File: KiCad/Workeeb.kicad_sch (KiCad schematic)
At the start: 224 parts, among them J1 USB_C_Receptacle_USB2.0, U1 EFM32HG322F64G-C-QFP48

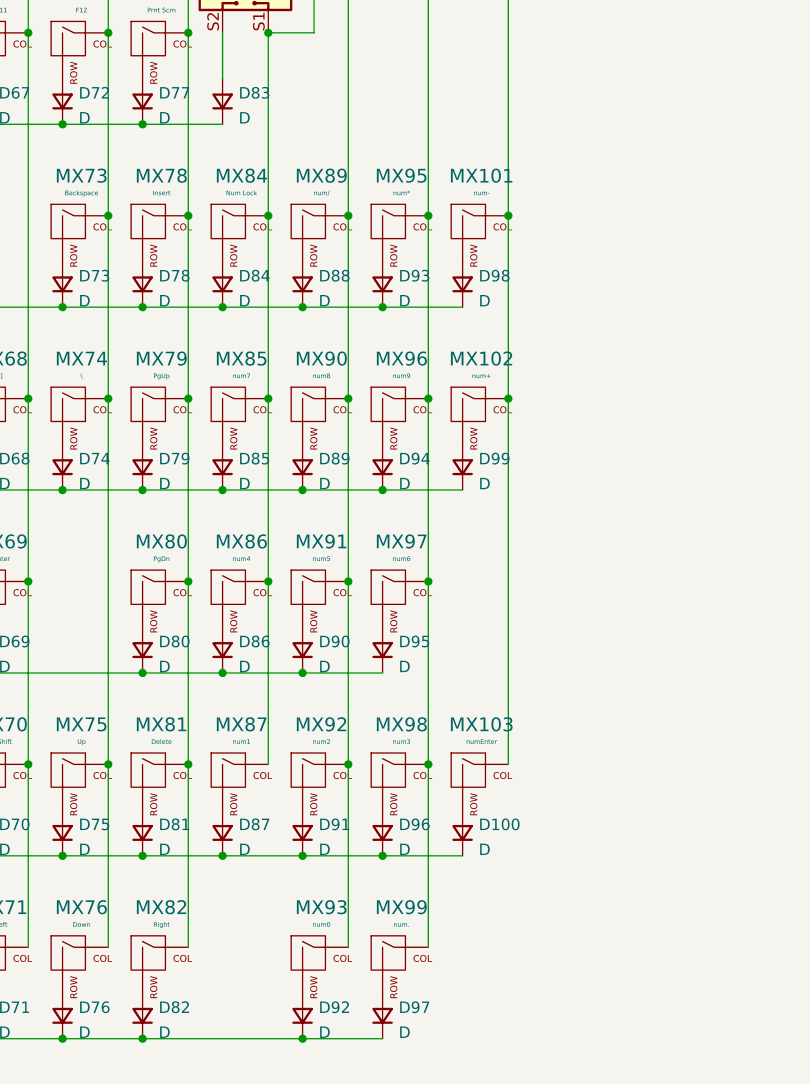
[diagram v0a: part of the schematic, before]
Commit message: Place all diodes and fix switch annotations
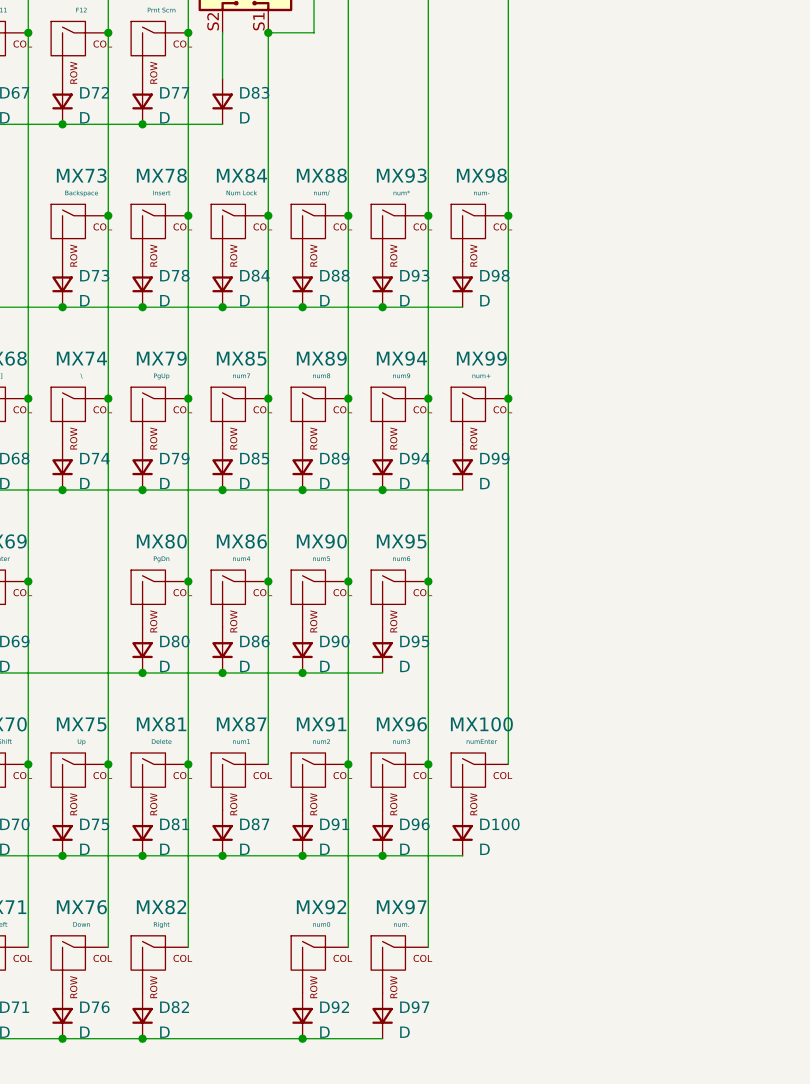
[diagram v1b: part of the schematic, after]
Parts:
- renumbered MX103 to MX100, MX89 to MX88, MX90 to MX89, MX91 to MX90, MX92 to MX91, MX93 to MX92, MX95 to MX93, MX96 to MX94, MX97 to MX95, MX98 to MX96, MX99 to MX97, MX101 to MX98, MX102 to MX99
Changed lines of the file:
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@@
   (symbol (lib_id "Workeeb-rescue:MX-NoLED-MX_Alps_Hybrid") (at 184.15 59.69 0) (unit 1)
     (in_bom yes) (on_board yes)
-    (property "Reference" "MX89" (id 0) (at 184.9882 54.0258 0)
+    (property "Reference" "MX88" (id 0) (at 184.9882 54.0258 0)
       (effects (font (size 1.524 1.524)))
     )
@@
   (symbol (lib_id "Workeeb-rescue:MX-NoLED-MX_Alps_Hybrid") (at 184.15 80.01 0) (unit 1)
     (in_bom yes) (on_board yes)
-    (property "Reference" "MX90" (id 0) (at 184.9882 74.3458 0)
+    (property "Reference" "MX89" (id 0) (at 184.9882 74.3458 0)
       (effects (font (size 1.524 1.524)))
     )
@@
   (symbol (lib_id "Workeeb-rescue:MX-NoLED-MX_Alps_Hybrid") (at 184.15 100.33 0) (unit 1)
     (in_bom yes) (on_board yes)
-    (property "Reference" "MX91" (id 0) (at 184.9882 94.6658 0)
+    (property "Reference" "MX90" (id 0) (at 184.9882 94.6658 0)
       (effects (font (size 1.524 1.524)))
     )
@@
   (symbol (lib_id "Workeeb-rescue:MX-NoLED-MX_Alps_Hybrid") (at 184.15 120.65 0) (unit 1)
     (in_bom yes) (on_board yes)
-    (property "Reference" "MX92" (id 0) (at 184.9882 114.9858 0)
+    (property "Reference" "MX91" (id 0) (at 184.9882 114.9858 0)
       (effects (font (size 1.524 1.524)))
     )
@@
   (symbol (lib_id "Workeeb-rescue:MX-NoLED-MX_Alps_Hybrid") (at 184.15 140.97 0) (unit 1)
     (in_bom yes) (on_board yes)
-    (property "Reference" "MX93" (id 0) (at 184.9882 135.3058 0)
+    (property "Reference" "MX92" (id 0) (at 184.9882 135.3058 0)
       (effects (font (size 1.524 1.524)))
     )
@@
   (symbol (lib_id "Workeeb-rescue:MX-NoLED-MX_Alps_Hybrid") (at 193.04 59.69 0) (unit 1)
     (in_bom yes) (on_board yes)
-    (property "Reference" "MX95" (id 0) (at 193.8782 54.0258 0)
+    (property "Reference" "MX93" (id 0) (at 193.8782 54.0258 0)
       (effects (font (size 1.524 1.524)))
     )
@@
   (symbol (lib_id "Workeeb-rescue:MX-NoLED-MX_Alps_Hybrid") (at 193.04 80.01 0) (unit 1)
     (in_bom yes) (on_board yes)
-    (property "Reference" "MX96" (id 0) (at 193.8782 74.3458 0)
+    (property "Reference" "MX94" (id 0) (at 193.8782 74.3458 0)
       (effects (font (size 1.524 1.524)))
     )
@@
   (symbol (lib_id "Workeeb-rescue:MX-NoLED-MX_Alps_Hybrid") (at 193.04 100.33 0) (unit 1)
     (in_bom yes) (on_board yes)
-    (property "Reference" "MX97" (id 0) (at 193.8782 94.6658 0)
+    (property "Reference" "MX95" (id 0) (at 193.8782 94.6658 0)
       (effects (font (size 1.524 1.524)))
     )
@@
   (symbol (lib_id "Workeeb-rescue:MX-NoLED-MX_Alps_Hybrid") (at 193.04 120.65 0) (unit 1)
     (in_bom yes) (on_board yes)
-    (property "Reference" "MX98" (id 0) (at 193.8782 114.9858 0)
+    (property "Reference" "MX96" (id 0) (at 193.8782 114.9858 0)
       (effects (font (size 1.524 1.524)))
     )
@@
   (symbol (lib_id "Workeeb-rescue:MX-NoLED-MX_Alps_Hybrid") (at 193.04 140.97 0) (unit 1)
     (in_bom yes) (on_board yes)
-    (property "Reference" "MX99" (id 0) (at 193.8782 135.3058 0)
+    (property "Reference" "MX97" (id 0) (at 193.8782 135.3058 0)
       (effects (font (size 1.524 1.524)))
     )
@@
   (symbol (lib_id "Workeeb-rescue:MX-NoLED-MX_Alps_Hybrid") (at 201.93 59.69 0) (unit 1)
     (in_bom yes) (on_board yes)
-    (property "Reference" "MX101" (id 0) (at 202.7682 54.0258 0)
+    (property "Reference" "MX98" (id 0) (at 202.7682 54.0258 0)
       (effects (font (size 1.524 1.524)))
     )
@@
   (symbol (lib_id "Workeeb-rescue:MX-NoLED-MX_Alps_Hybrid") (at 201.93 80.01 0) (unit 1)
     (in_bom yes) (on_board yes)
-    (property "Reference" "MX102" (id 0) (at 202.7682 74.3458 0)
+    (property "Reference" "MX99" (id 0) (at 202.7682 74.3458 0)
       (effects (font (size 1.524 1.524)))
     )
@@
   (symbol (lib_id "Workeeb-rescue:MX-NoLED-MX_Alps_Hybrid") (at 201.93 120.65 0) (unit 1)
     (in_bom yes) (on_board yes)
-    (property "Reference" "MX103" (id 0) (at 202.7682 114.9858 0)
+    (property "Reference" "MX100" (id 0) (at 202.7682 114.9858 0)
       (effects (font (size 1.524 1.524)))
     )
@@
     )
     (path "/00000000-0000-0000-0000-000061a51198"
-      (reference "MX89") (unit 1) (value "num/") (footprint "MX_Only:MXOnly-1U-NoLED")
+      (reference "MX88") (unit 1) (value "num/") (footprint "MX_Only:MXOnly-1U-NoLED")
     )
     (path "/00000000-0000-0000-0000-000061a5119e"
-      (reference "MX90") (unit 1) (value "num8") (footprint "MX_Only:MXOnly-1U-NoLED")
+      (reference "MX89") (unit 1) (value "num8") (footprint "MX_Only:MXOnly-1U-NoLED")
     )
     (path "/00000000-0000-0000-0000-000061a511a4"
-      (reference "MX91") (unit 1) (value "num5") (footprint "MX_Only:MXOnly-1U-NoLED")
+      (reference "MX90") (unit 1) (value "num5") (footprint "MX_Only:MXOnly-1U-NoLED")
     )
     (path "/00000000-0000-0000-0000-000061a511aa"
-      (reference "MX92") (unit 1) (value "num2") (footprint "MX_Only:MXOnly-1U-NoLED")
+      (reference "MX91") (unit 1) (value "num2") (footprint "MX_Only:MXOnly-1U-NoLED")
     )
     (path "/00000000-0000-0000-0000-000061a511b0"
-      (reference "MX93") (unit 1) (value "num0") (footprint "MX_Only:MXOnly-2U-NoLED")
+      (reference "MX92") (unit 1) (value "num0") (footprint "MX_Only:MXOnly-2U-NoLED")
     )
     (path "/00000000-0000-0000-0000-000061a53634"
-      (reference "MX95") (unit 1) (value "num*") (footprint "MX_Only:MXOnly-1U-NoLED")
+      (reference "MX93") (unit 1) (value "num*") (footprint "MX_Only:MXOnly-1U-NoLED")
     )
     (path "/00000000-0000-0000-0000-000061a5363a"
-      (reference "MX96") (unit 1) (value "num9") (footprint "MX_Only:MXOnly-1U-NoLED")
+      (reference "MX94") (unit 1) (value "num9") (footprint "MX_Only:MXOnly-1U-NoLED")
     )
     (path "/00000000-0000-0000-0000-000061a53640"
-      (reference "MX97") (unit 1) (value "num6") (footprint "MX_Only:MXOnly-1U-NoLED")
+      (reference "MX95") (unit 1) (value "num6") (footprint "MX_Only:MXOnly-1U-NoLED")
     )
     (path "/00000000-0000-0000-0000-000061a53646"
-      (reference "MX98") (unit 1) (value "num3") (footprint "MX_Only:MXOnly-1U-NoLED")
+      (reference "MX96") (unit 1) (value "num3") (footprint "MX_Only:MXOnly-1U-NoLED")
     )
     (path "/00000000-0000-0000-0000-000061a5364c"
-      (reference "MX99") (unit 1) (value "num.") (footprint "MX_Only:MXOnly-1U-NoLED")
+      (reference "MX97") (unit 1) (value "num.") (footprint "MX_Only:MXOnly-1U-NoLED")
     )
     (path "/00000000-0000-0000-0000-000061a54448"
-      (reference "MX101") (unit 1) (value "num-") (footprint "MX_Only:MXOnly-1U-NoLED")
+      (reference "MX98") (unit 1) (value "num-") (footprint "MX_Only:MXOnly-1U-NoLED")
     )
     (path "/00000000-0000-0000-0000-000061a5444e"
-      (reference "MX102") (unit 1) (value "num+") (footprint "MX_Only:MXOnly-2U-VerticalStabilizers-NoLED")
+      (reference "MX99") (unit 1) (value "num+") (footprint "MX_Only:MXOnly-2U-VerticalStabilizers-NoLED")
     )
     (path "/00000000-0000-0000-0000-000061a544c8"
-      (reference "MX103") (unit 1) (value "numEnter") (footprint "MX_Only:MXOnly-2U-VerticalStabilizers-NoLED")
+      (reference "MX100") (unit 1) (value "numEnter") (footprint "MX_Only:MXOnly-2U-VerticalStabilizers-NoLED")
     )
     (path "/d05027c8-0e1d-4baf-8884-af7434122815"

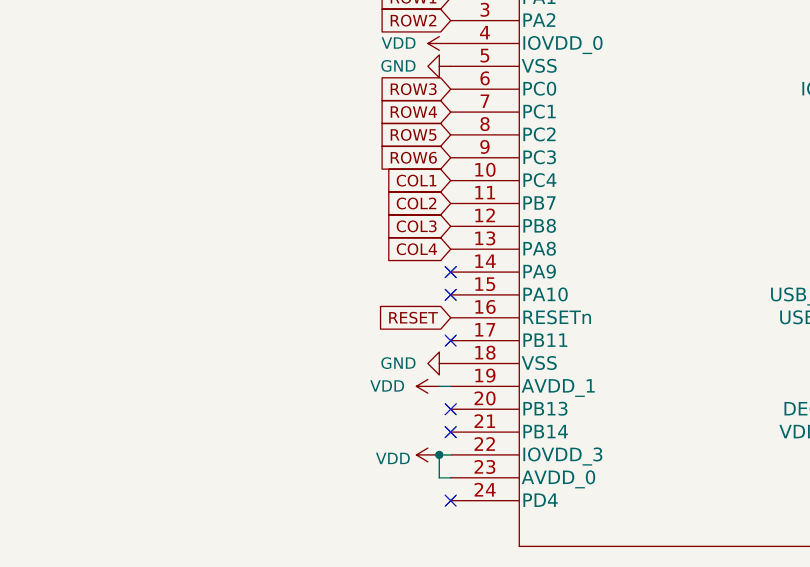
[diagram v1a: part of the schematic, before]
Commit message: Route all left-side cols to MCU area
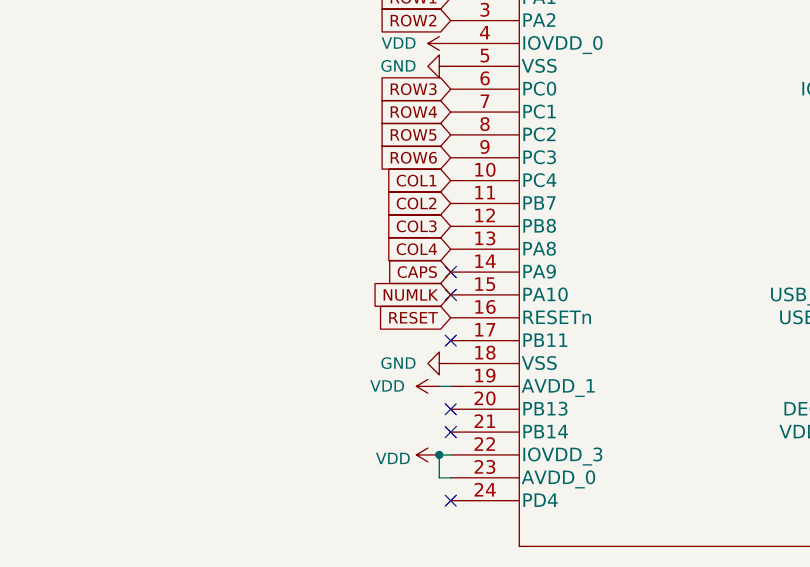
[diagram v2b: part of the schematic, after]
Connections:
- net CAPS: now reaches U1.14 (PA9)
- net NUMLK: now reaches U1.15 (PA10)
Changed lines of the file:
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@@
+    )
+  )
+  (global_label "CAPS" (shape input) (at 308.61 82.55 180) (fields_autoplaced)
+    (effects (font (size 1.27 1.27)) (justify right))
+    (property "Intersheet References" "${INTERSHEET_REFS}" (id 0) (at 301.4477 82.4706 0)
+      (effects (font (size 1.27 1.27)) (justify right) hide)
     )
   )
@@
       (effects (font (size 1.27 1.27)) (justify right) hide)
     )
+  )
+  (global_label "NUMLK" (shape input) (at 308.61 85.09 180) (fields_autoplaced)
+    (effects (font (size 1.27 1.27)) (justify right))
+    (property "Intersheet References" "${INTERSHEET_REFS}" (id 0) (at 299.8753 85.0106 0)
+      (effects (font (size 1.27 1.27)) (justify right) hide)
+    )

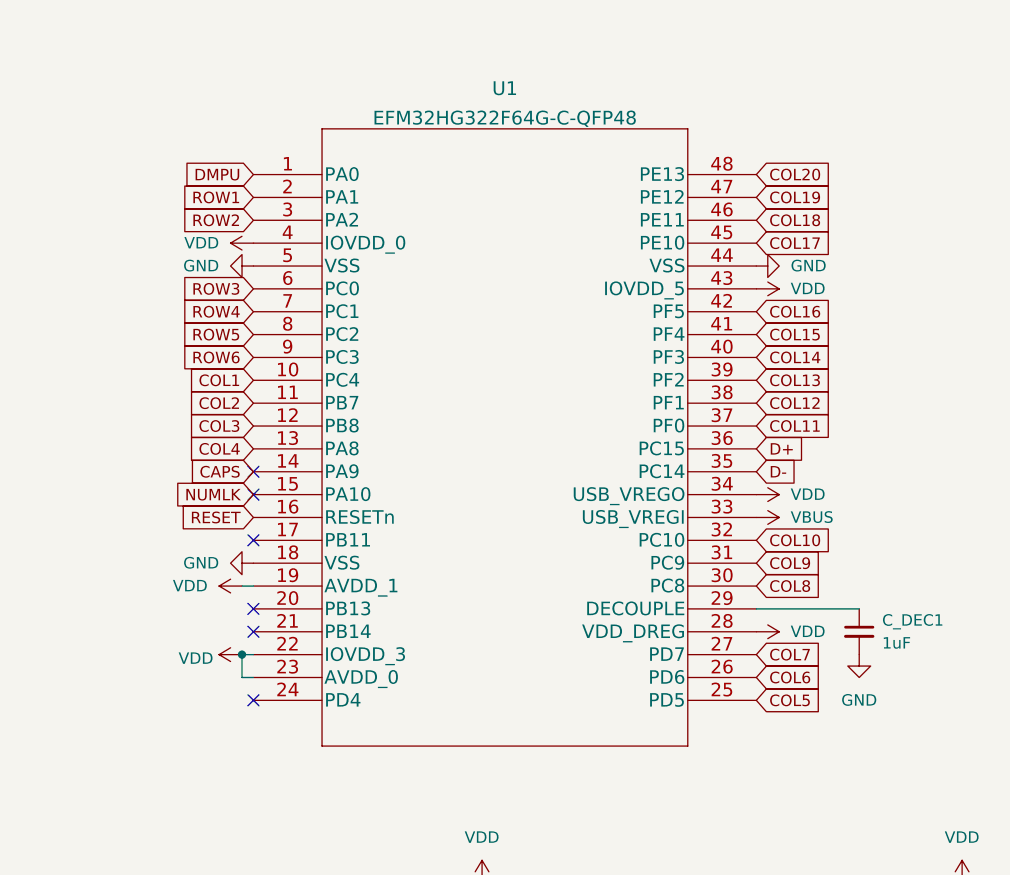
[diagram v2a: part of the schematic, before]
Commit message: Reorder row/cols to match physical layout of routes better
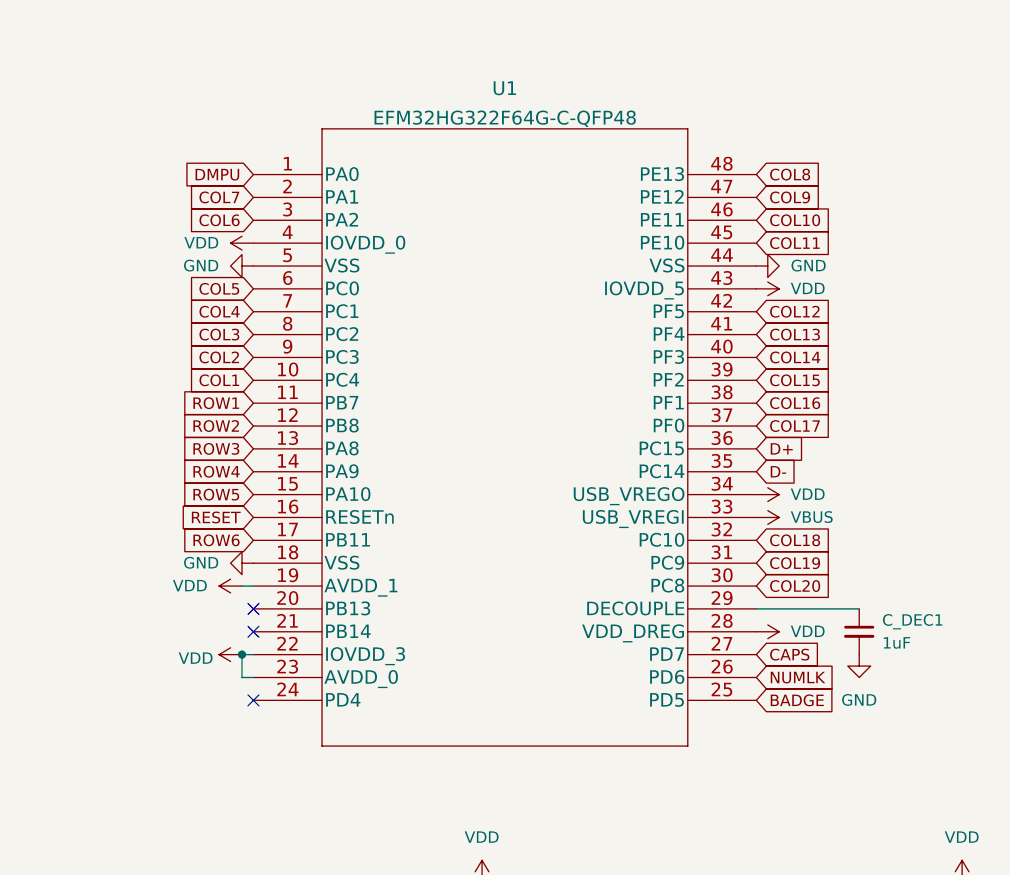
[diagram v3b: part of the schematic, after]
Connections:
- net CAPS: now also U1.27 (PD7); no longer U1.14 (PA9)
- net COL10: now also U1.46 (PE11); no longer U1.32 (PC10)
- net COL11: now also U1.45 (PE10); no longer U1.37 (PF0)
- net COL12: now also U1.42 (PF5); no longer U1.38 (PF1)
- net COL13: now also U1.41 (PF4); no longer U1.39 (PF2)
- net COL15: now also U1.39 (PF2); no longer U1.41 (PF4)
- net COL16: now also U1.38 (PF1); no longer U1.42 (PF5)
- net COL17: now also U1.37 (PF0); no longer U1.45 (PE10)
- net COL18: now also U1.32 (PC10); no longer U1.46 (PE11)
- net COL19: now also U1.31 (PC9); no longer U1.47 (PE12)
- net COL2: now also U1.9 (PC3); no longer U1.11 (PB7)
- net COL20: now also U1.30 (PC8); no longer U1.48 (PE13)
- net COL3: now also U1.8 (PC2); no longer U1.12 (PB8)
- net COL4: now also U1.7 (PC1); no longer U1.13 (PA8)
- net COL5: now also U1.6 (PC0); no longer U1.25 (PD5)
- net COL6: now also U1.3 (PA2); no longer U1.26 (PD6)
- net COL7: now also U1.2 (PA1); no longer U1.27 (PD7)
- net COL8: now also U1.48 (PE13); no longer U1.30 (PC8)
- net COL9: now also U1.47 (PE12); no longer U1.31 (PC9)
- net NUMLK: now also U1.26 (PD6); no longer U1.15 (PA10)
- net ROW1: now also U1.11 (PB7); no longer U1.2 (PA1)
- net ROW2: now also U1.12 (PB8); no longer U1.3 (PA2)
- net ROW3: now also U1.13 (PA8); no longer U1.6 (PC0)
- net ROW4: now also U1.14 (PA9); no longer U1.7 (PC1)
- net ROW5: now also U1.15 (PA10); no longer U1.8 (PC2)
- net ROW6: now also U1.17 (PB11); no longer U1.9 (PC3)
- new net BADGE: U1.25 (PD5)
- no-connect marks 8 -> 5

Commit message: Start to do power routing
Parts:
- added D101: SK6812, LED_SMD:LED_SK6812_PLCC4_5.0x5.0mm_P3.2mm, symbol LED:SK6812
- added D102, D103: LED, LED_SMD:LED_1206_3216Metric_Pad1.42x1.75mm_HandSolder, symbol Device:LED
- renumbered C_AVDD_0 to C_AVDD_1, C_AVDD_1 to C_AVDD_2, C_IOVDD_0 to C_IOVDD_1, C_IOVDD_3 to C_IOVDD_2, C_IOVDD_5 to C_IOVDD_3, MX84 to MX83, MX85 to MX84, MX86 to MX85, MX87 to MX86, MX83 to MX87, R_CC2 to R_CC1, R_CC1 to R_CC2
